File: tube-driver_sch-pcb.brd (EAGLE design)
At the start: 100 x 100 mm, 108 parts, among them CN1 KS 54, CN10 NO FIT, CN2 MUSB-05-S-B-SM-A, CN3 KS 54, CN4 KS 54, CN5 KS 54, CN6 KS 54, CN7 KS 54, CN8 KS 54, CN9 KS 54, Q4 MMBT3904, Q5 MMBT3904, SW1 RA SM TACT, SW2 RA SM TACT, SW3 RA SM TACT, U1 STM32L052C8, U10 TPS61500, U2 TPS61500, U3 TPS61500, U5 ESP32, U6 USBLC6-2SC6, U7 FT231X, U8 TPS61500

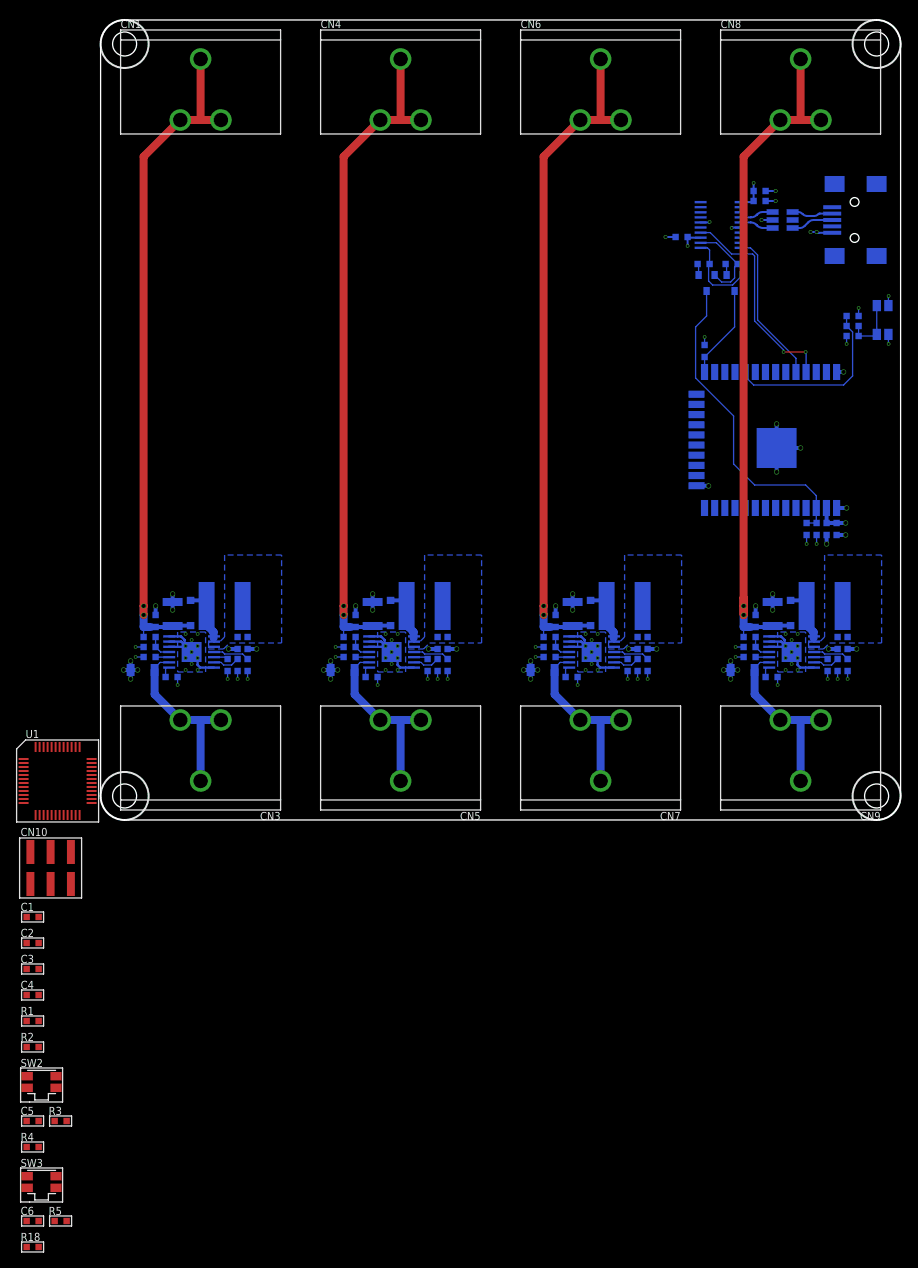
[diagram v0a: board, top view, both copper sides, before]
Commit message: First revision done, need to test ESP32 SPi
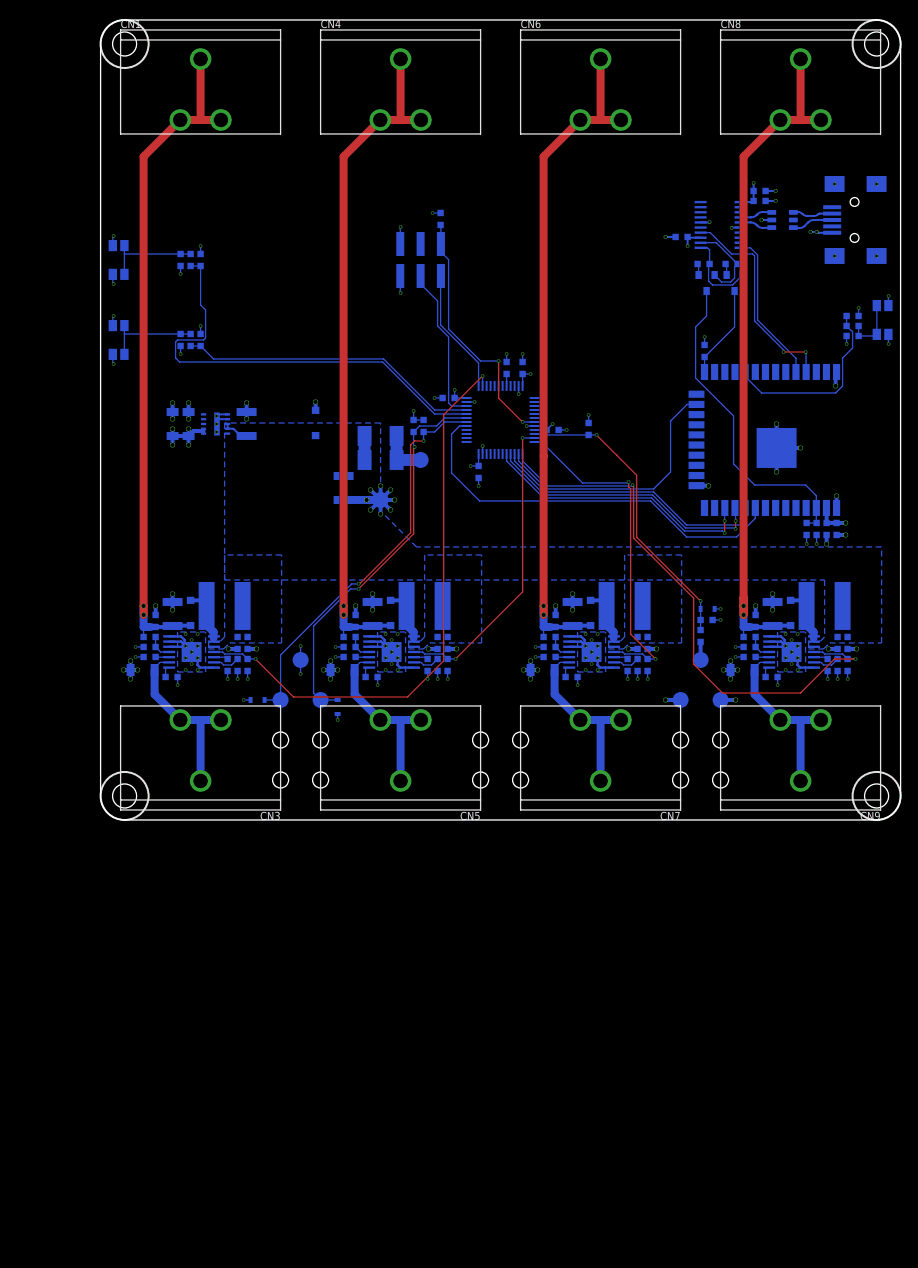
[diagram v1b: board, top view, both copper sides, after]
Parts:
- added C29, C30: 22uF 10V, CAPACITORS:1206
- added C31, C7: 10uF 50V, CAPACITORS:1210
- added C32: 1uF 25V, CAPACITORS:0603
- added D1, D4: B360A-13-F, DIODES:DO214AC
- added D10, D8, D9: PESD5Z3.3, DIODES:SC-79
- added D6: B0540W, DIODES:SOD-123
- added R23, R24: 10k, r_0603:0603
- added R25: 1.0k, r_0603:0603
- added R26: 100k, r_0603:0603
- added TP1, TP2, TP3, TP4, TP5, TP6, TP7, TP8: 2MM_TEST_POINT, MISC:2MM_TEST_PAD
- added U11: 3.3V BUCK, ICs:TI_MICROSIP_10
- moved R2 115.4 mm to (42.5, 75.1), flipped to the bottom, turned to 90 degrees
- moved R18 115.1 mm to (11.2, 60.0), flipped to the bottom, turned to 90 degrees
- moved R4 112.6 mm to (11.2, 70.0), flipped to the bottom, turned to 90 degrees
- moved C6 112.1 mm to (12.5, 60.0), flipped to the bottom, turned to 270 degrees
- moved R5 111.1 mm to (10.0, 60.0), flipped to the bottom, turned to 270 degrees
- moved C5 109.7 mm to (12.5, 70.0), flipped to the bottom, turned to 270 degrees
- moved R3 108.7 mm to (10.0, 70.0), flipped to the bottom, turned to 270 degrees
- moved SW3 105.7 mm to (2.25, 60.0), flipped to the bottom, turned to 90 degrees
- moved SW2 103.2 mm to (2.25, 70.0), flipped to the bottom, turned to 90 degrees
- moved R1 100.9 mm to (50.8, 56.5), flipped to the bottom, turned to 270 degrees
- moved C4 99.5 mm to (52.8, 56.5), flipped to the bottom, turned to 270 degrees
- moved C1 89.1 mm to (56.5, 48.8), flipped to the bottom
- moved CN10 89.0 mm to (40.0, 70.0), flipped to the bottom, turned to 180 degrees
- moved C3 88.3 mm to (43.5, 52.8), flipped to the bottom, turned to 180 degrees
- moved C2 81.1 mm to (47.2, 43.5), flipped to the bottom, turned to 90 degrees
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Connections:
- new net N$4: R25.1, TP7.1
- new net N$5: D1.A, D4.A, TP1.1
- net 3V3: now also C29.2, C30.2, R23.2, R24.2, TP6.1, U11.6, U11.7
- net DEBUG_UART_RX: now also D9.K, R24.1, TP4.1
- net DEBUG_UART_TX: now also D10.K, R23.1, TP3.1
- net GND: now also C29.1, C30.1, C31.1, C32.1, C7.1, D10.A, D6.A, D8.A, D9.A, R26.1, TP2.1, TP5.1, TP8.1, U11.1, U11.2, U11.PAD
- net VIN: now also C31.2, C7.2, D1.K, D4.K, D6.K, U11.3, U11.4
- net VOL_CONT: now also C32.2, D8.K, R25.2, R26.2
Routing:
- net LED_PWM_0: track 4.56 -> 71.8 mm, vias 0 -> 2
- net LED_PWM_3: track 4.56 -> 70.6 mm, vias 0 -> 2
- net GND: track 141.4 -> 199.3 mm, vias 124 -> 170
- net USER_BTN_0: track 0.00 -> 55.7 mm
- net ESP_INT: track 0.00 -> 50.7 mm
- net DEBUG_UART_TX: track 0.00 -> 50.0 mm, vias 0 -> 2
- net DEBUG_UART_RX: track 0.00 -> 49.2 mm, vias 0 -> 2
- net LED_PWM_2: track 4.56 -> 43.0 mm, vias 0 -> 2
- net USER_BTN_1: track 0.00 -> 37.8 mm
- net VOL_CONT: track 0.00 -> 37.6 mm, vias 0 -> 2
- net ESP_SPI_MISO: track 0.00 -> 35.4 mm, vias 0 -> 2
- net ESP_SPI_MOSI: track 0.00 -> 35.0 mm, vias 0 -> 2
- net ESP_SPI_SCLK: track 0.00 -> 34.8 mm
- net LED_PWM_1: track 4.56 -> 38.2 mm, vias 0 -> 2
- net ESP_SPI_CS: track 0.00 -> 32.7 mm
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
